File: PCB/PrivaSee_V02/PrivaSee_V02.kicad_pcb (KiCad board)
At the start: 4 copper layers, 69.8 x 90 mm, 31 parts, among them J1 RFPC-SMA27-F, J2 Batt_Solder_Point, J3 Conn_02x06_Odd_Even, J4 VOUT_TEST, J5 GND_TEST, J6 IR_TEST, J7 RF_TEST, SW1 Switch, SW2 SW_Push, U2 LM358, U3 254, U4 DFR0568, U6 ESP32-C5-DevKitC-1

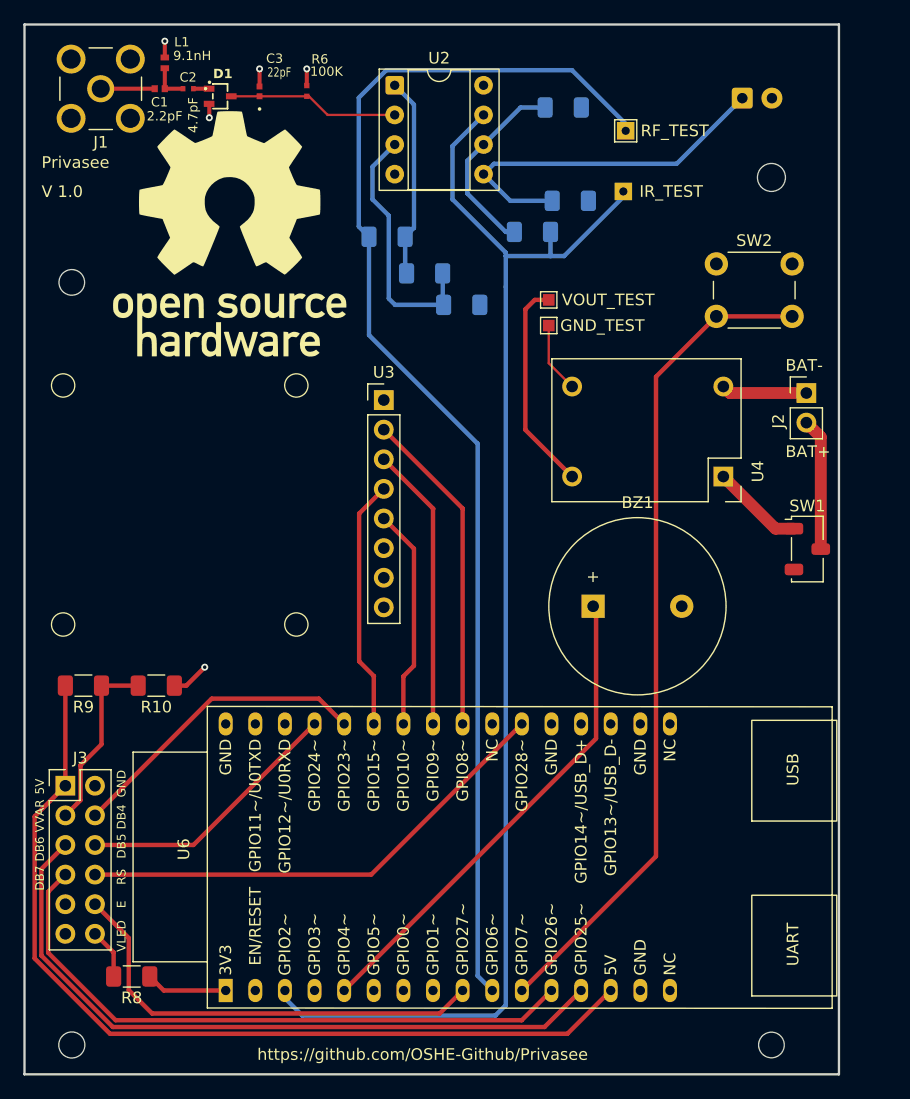
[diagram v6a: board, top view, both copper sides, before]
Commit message: More edits
Rerouting traces, pull down resistor added (I believe thats the right way for a pull down resistor). Creating more spacing between traces.
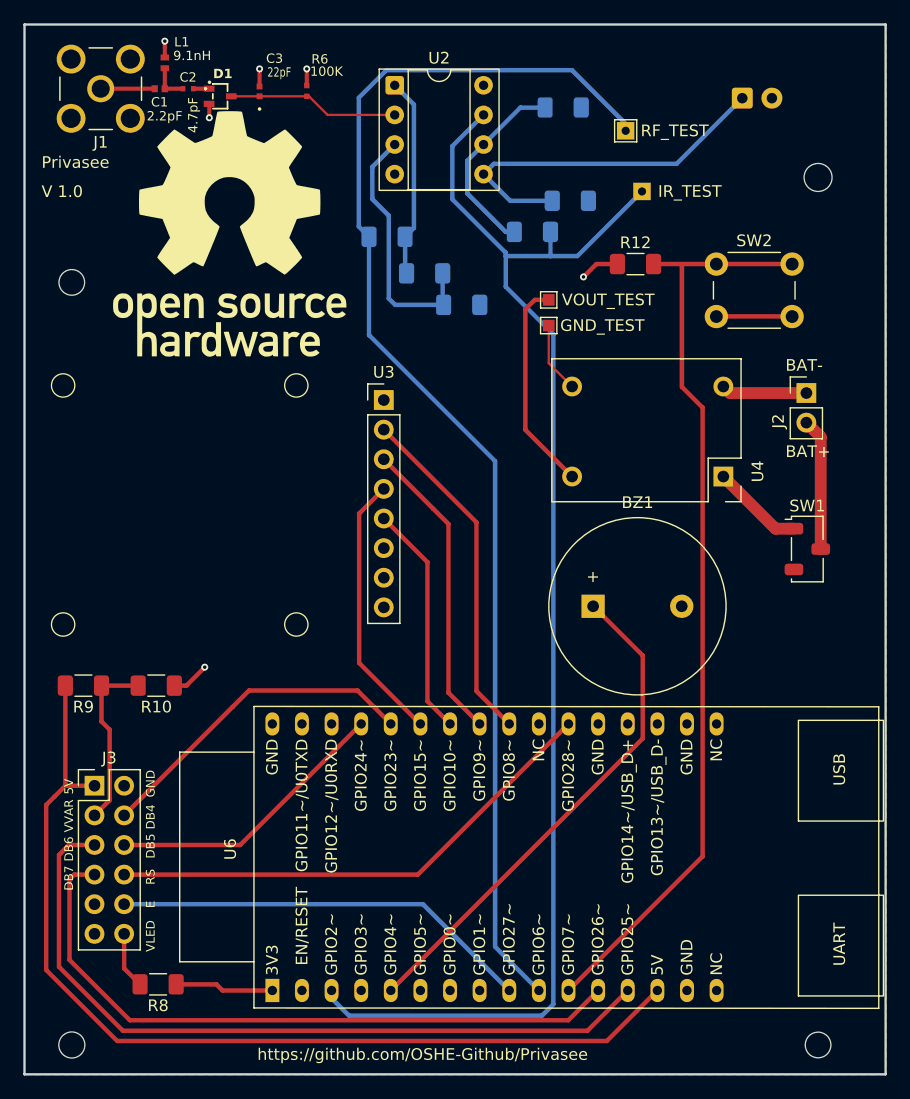
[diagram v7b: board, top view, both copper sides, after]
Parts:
- added R12: 10k, Resistor_SMD:R_1206_3216Metric_Pad1.30x1.75mm_HandSolder, F.Cu at (118.4, 42.1)
- moved U6 4.00 mm to (87.3, 104.5)
- moved J3 2.50 mm to (72.0, 86.9)
- moved R8 2.36 mm to (77.5, 103.9)
- moved J6 1.60 mm to (119.0, 35.9)
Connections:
- SW2 pad 1: GND -> Net-(U6-GPIO7)
- SW2 pad 2: Net-(U6-GPIO7) -> /3V3
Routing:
- net Net-(U6-GPIO7): track 71.2 -> 79.7 mm
- net /3V3: track 25.4 -> 33.3 mm
- net 5V: track 78.1 -> 84.3 mm
- net LCD_DB6: track 60.5 -> 65.5 mm
- net LCD_DB7: track 53.9 -> 57.8 mm
- net GND: track 15.0 -> 18.3 mm, vias 5 -> 6
- net Net-(J6-Pin_1): track 114.7 -> 117.7 mm
- net LCD_E: track 38.8 -> 36.1 mm
- net LCD_DB4: track 26.4 -> 28.5 mm
- net Net-(BZ1-+): track 42.0 -> 44.0 mm
- net Net-(U3-DI): track 24.5 -> 26.1 mm
- net Net-(U3-DO): track 21.6 -> 23.2 mm
- net Net-(J7-Pin_1): track 108.0 -> 109.7 mm
- net Net-(U3-CS): track 28.1 -> 29.7 mm
- net LCD_RS: track 42.0 -> 43.5 mm
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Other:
- board size 69.8 x 90 mm -> 73.8 x 90 mm

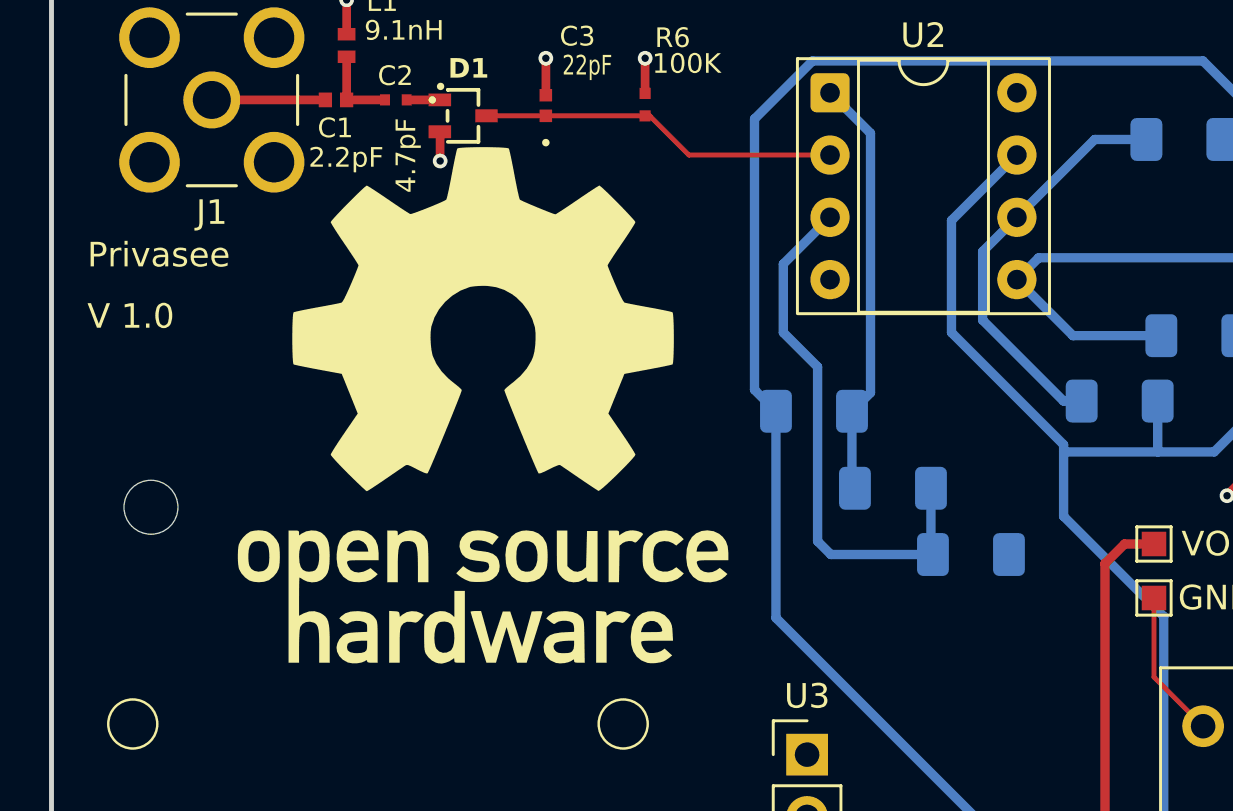
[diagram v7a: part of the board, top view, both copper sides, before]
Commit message: Updates to PCB resize logo, reroute a couple traces under Eric's advice, etc
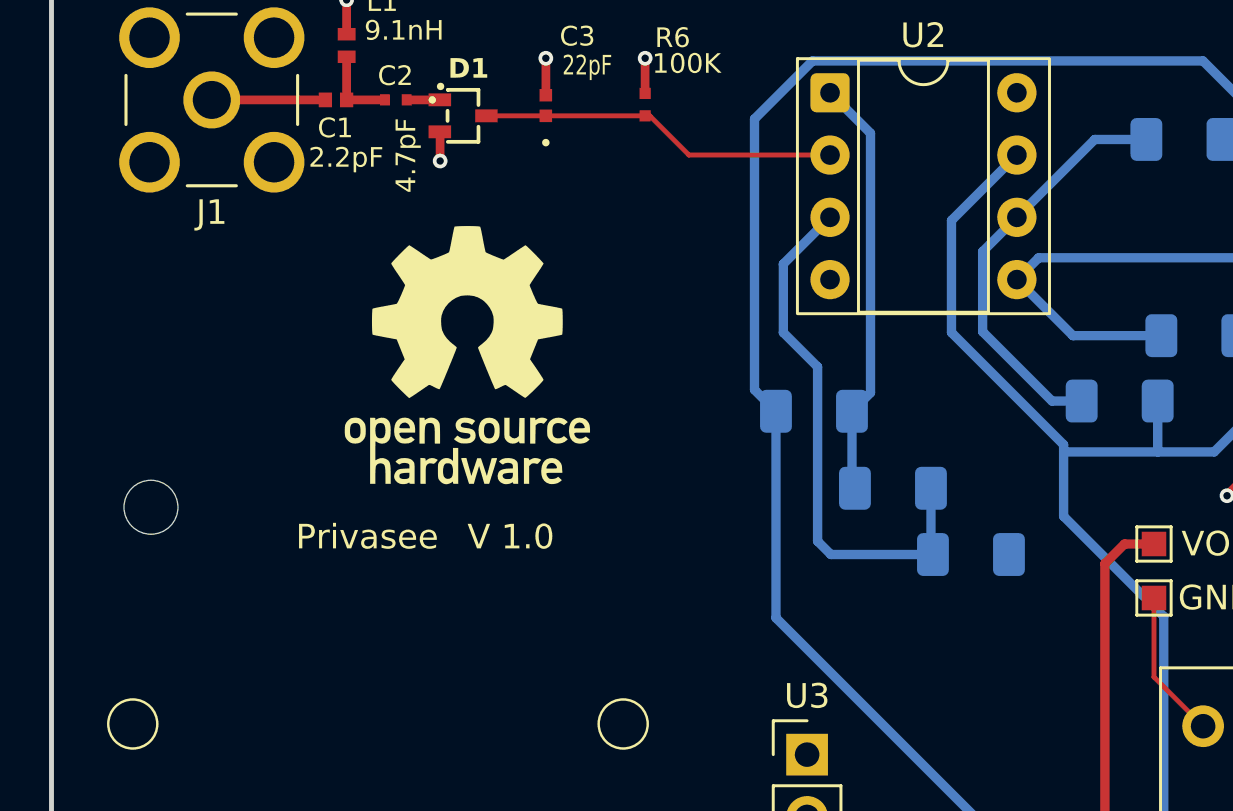
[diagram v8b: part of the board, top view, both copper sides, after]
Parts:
- moved ? 2.15 mm to (83.0, 37.5)
